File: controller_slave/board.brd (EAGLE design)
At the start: 85.1 x 67 mm, 60 parts, among them IC1 74HC595N, IC2 74HC595N, IC3 74HC595N, IC4 7805TV, Q1 14,7456, U1 ATTINY85-20P, X1 MKDSN1,5/2-5,08, X2 MKDSN1,5/2-5,08, X3 MKDSN1,5/2-5,08

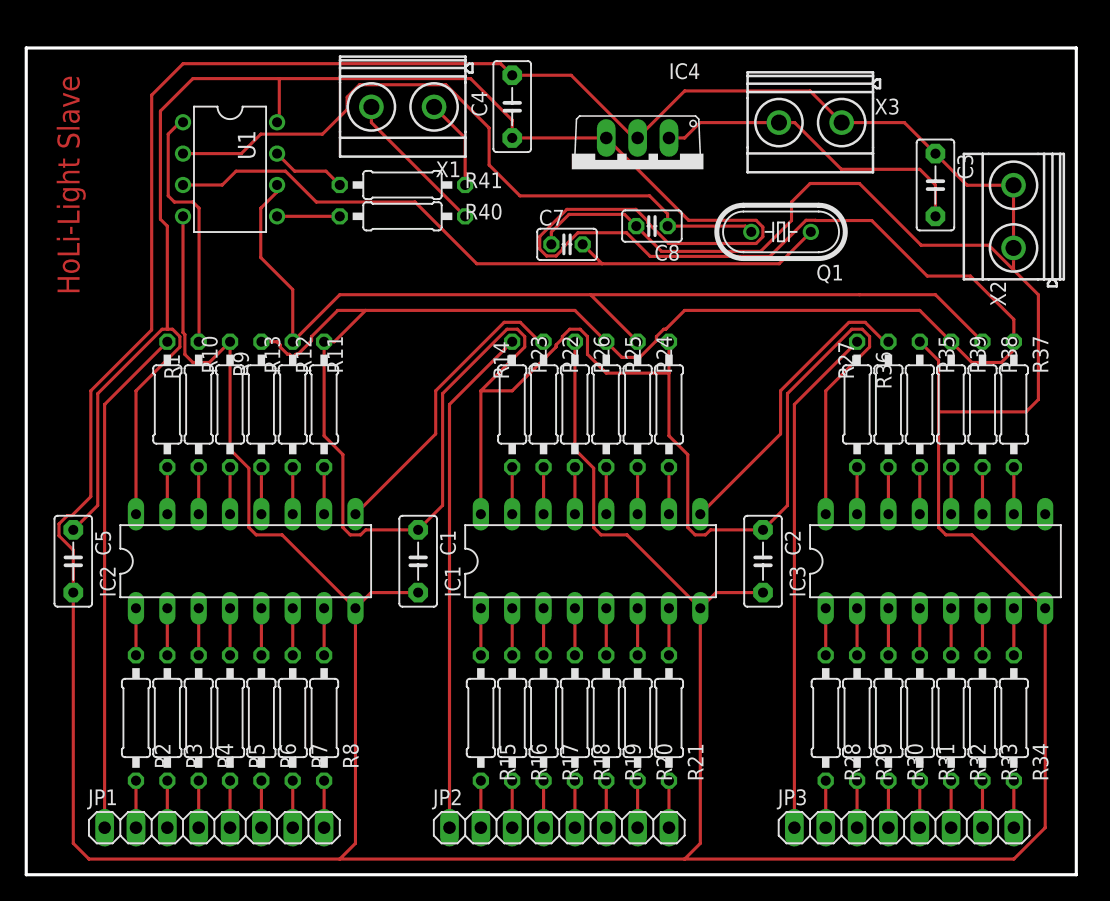
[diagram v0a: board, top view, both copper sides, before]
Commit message: update slave pcb: better connection to quarz
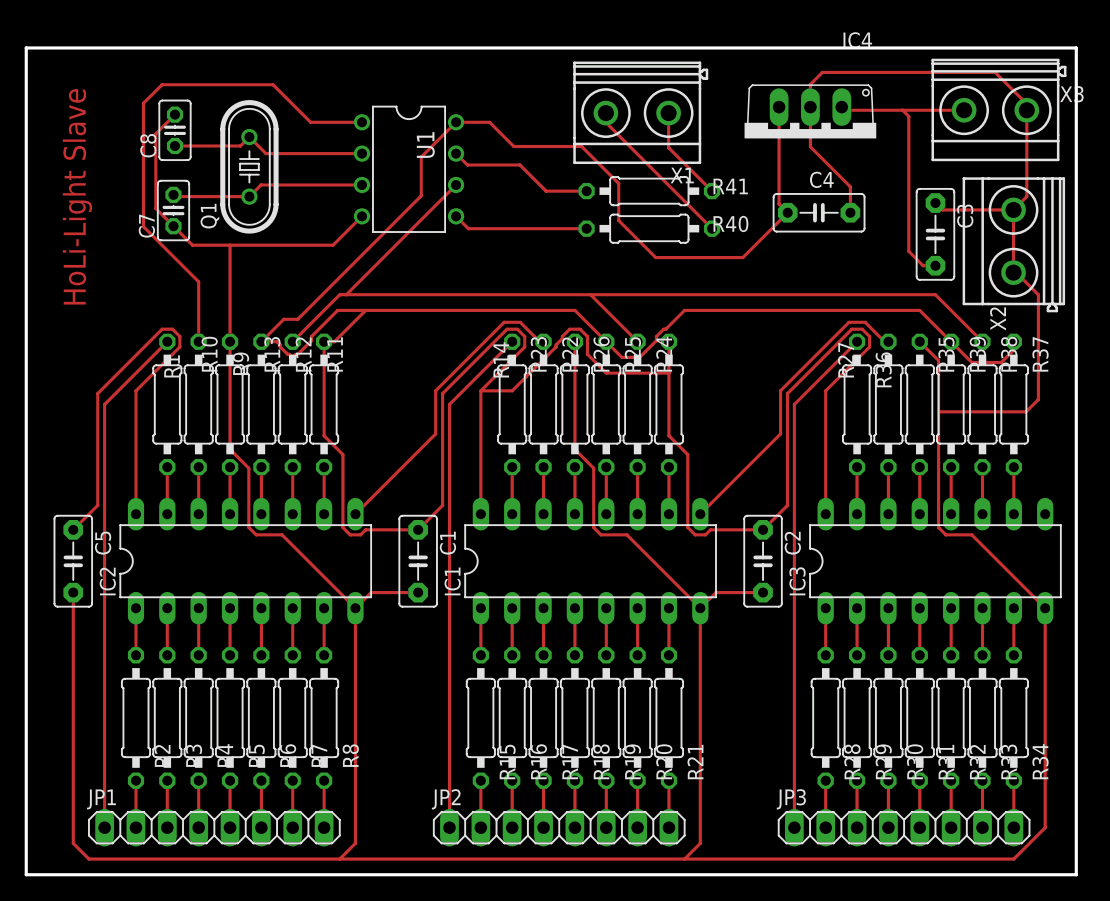
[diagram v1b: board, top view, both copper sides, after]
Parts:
- moved Q1 43.4 mm to (18.1, 57.4), turned to 90 degrees
- moved C8 39.4 mm to (12.1, 60.3), turned to 90 degrees
- moved C7 32.0 mm to (11.9, 53.8), turned to 90 degrees
- moved C4 26.3 mm to (64.2, 53.6), turned to 180 degrees
- moved R40 20.0 mm to (50.5, 52.3)
- moved R41 20.0 mm to (50.5, 55.4)
- moved X1 19.0 mm to (49.5, 61.7)
- moved X3 15.0 mm to (78.5, 62.0)
- moved U1 14.5 mm to (31.0, 57.1)
- moved IC4 14.2 mm to (63.5, 59.6)
- moved C3 4.00 mm to (73.7, 51.9)
- moved X2 2.00 mm to (80.0, 51.3)
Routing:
- net GND: track 463.5 -> 358.5 mm
- net +5V: track 394.8 -> 318.3 mm
- net N$74: track 57.7 -> 15.7 mm
- net N$78: track 56.2 -> 16.0 mm
- net N$73: track 20.3 -> 40.8 mm
- net N$69: track 5.08 -> 11.0 mm
- net N$70: track 6.13 -> 11.8 mm
- net N$72: track 26.7 -> 24.3 mm
- net N$67: track 78.7 -> 77.0 mm
- net N$66: track 12.0 -> 12.9 mm
